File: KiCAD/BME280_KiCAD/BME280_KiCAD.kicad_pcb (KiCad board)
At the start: 2 copper layers, 22 parts, among them Q1 2N7000, Q2 2N7000, Q3 2N7000, U1 D148K, U2 ESP32-S3-DevKitC, U3 D148K, U4 D148K, U5 2652

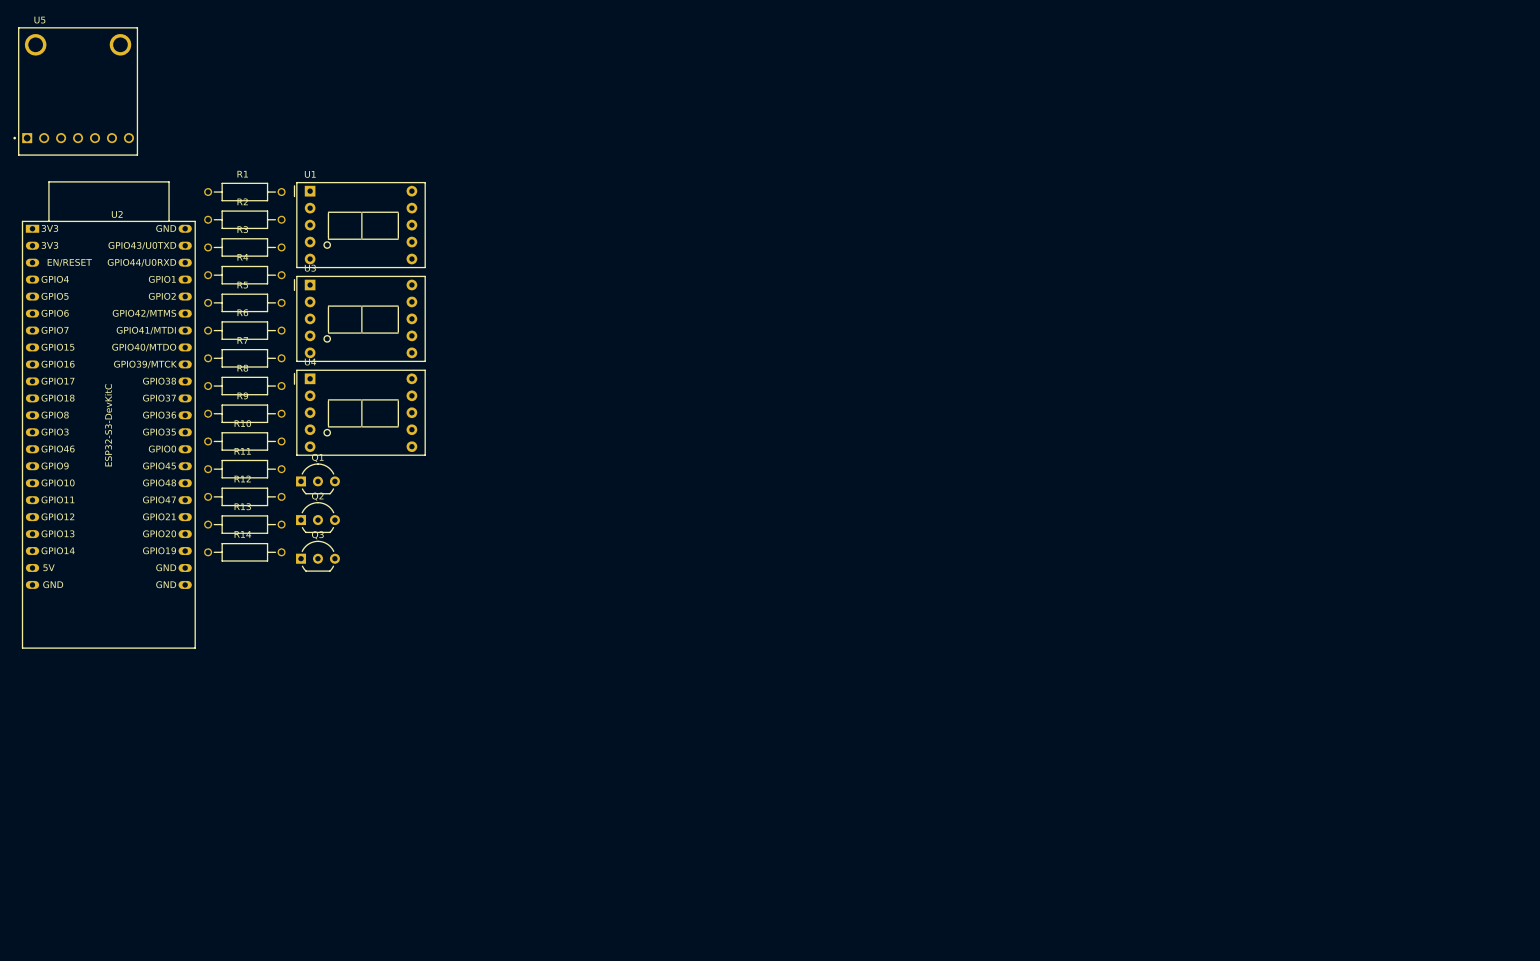
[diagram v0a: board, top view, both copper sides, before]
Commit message: made I2C oled display work without library, next time will use adafruit library
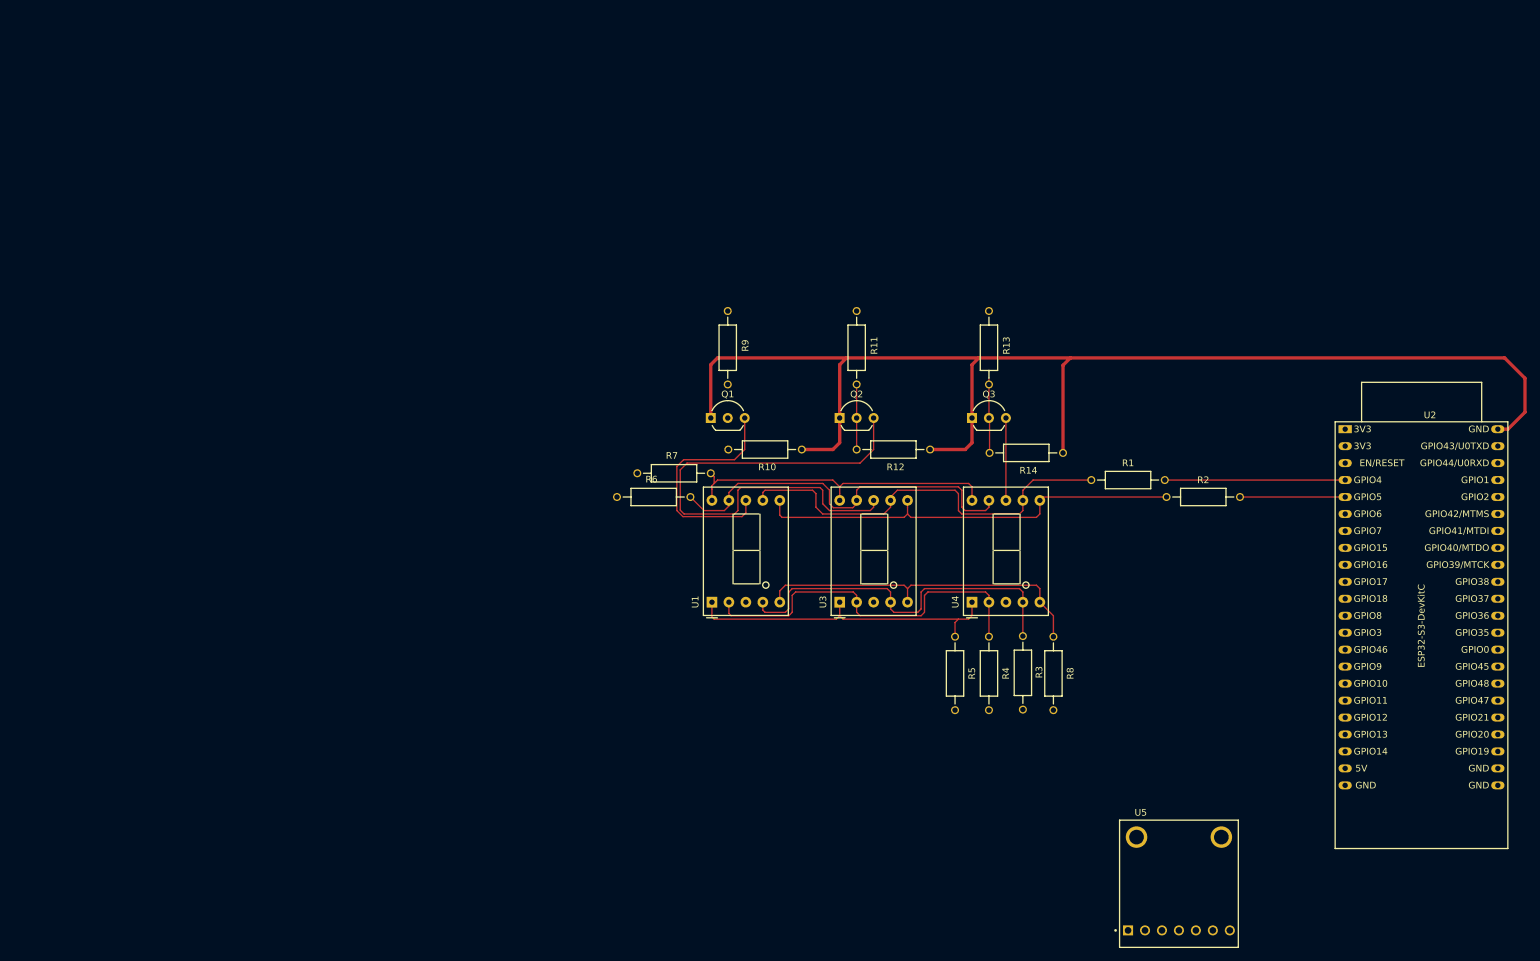
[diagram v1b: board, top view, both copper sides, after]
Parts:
- U2: footprint esp32_local:ESP32-S3-DevKitC -> esp32:ESP32-S3
- moved U5 203.1 mm to (173.2, 105.2)
- moved U2 198.8 mm to (198.1, 37.1)
- moved R2 149.4 mm to (176.9, 47.2), turned to 180 degrees
- moved R1 139.1 mm to (165.6, 44.7), turned to 180 degrees
- moved R3 132.8 mm to (149.9, 73.6), turned to 90 degrees
- moved R8 128.5 mm to (154.4, 73.7), turned to 90 degrees
- moved R4 126.4 mm to (144.8, 73.7), turned to 90 degrees
- moved R5 119.9 mm to (139.7, 73.7), turned to 90 degrees
- moved R14 118.0 mm to (150.4, 40.6), turned to 180 degrees
- moved R13 114.5 mm to (144.8, 24.9), turned to -90 degrees
- moved U4 104.6 mm to (142.2, 63.0), turned to 90 degrees
- moved Q3 102.7 mm to (142.2, 35.4)
- moved R12 97.4 mm to (130.5, 40.1), turned to 180 degrees
- moved R11 93.4 mm to (125.0, 24.9), turned to -90 degrees
- moved U3 92.4 mm to (122.4, 63.0), turned to 90 degrees
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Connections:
- Q1 pad 1: GNDREF -> GND
- Q2 pad 1: GNDREF -> GND
- Q3 pad 1: GNDREF -> GND
- U5 pad 5: unconnected-(U5-SDO-Pad5) -> VCC (3.3V)
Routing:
- net GND: track 0.00 -> 195.5 mm
- net Net-(Q2-D): track 0.00 -> 77.4 mm
- net Net-(U1-B): track 0.00 -> 65.2 mm
- net Net-(U1-A): track 0.00 -> 62.4 mm
- net Net-(U1-F): track 0.00 -> 57.8 mm
- net Net-(U1-D): track 0.00 -> 56.1 mm
- net Net-(U1-C): track 0.00 -> 56.0 mm
- net Net-(U1-DP): track 0.00 -> 51.7 mm
- net Net-(U1-E): track 0.00 -> 48.8 mm
- net Net-(U1-G): track 0.00 -> 48.1 mm
- net Net-(Q1-D): track 0.00 -> 35.3 mm
- net GPIO 4: track 0.00 -> 27.0 mm
- net GPIO 5: track 0.00 -> 15.7 mm
- net Net-(Q3-D): track 0.00 -> 12.3 mm
- net Net-(Q3-G): track 0.00 -> 11.3 mm
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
